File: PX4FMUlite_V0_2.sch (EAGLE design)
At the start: 150 parts, among them J2 DF13-4P-1.25V, J201 DF13C-6P-1.25V, J202 DF13C-6P-1.25V, J203 DF13C-6P-1.25V, J301 47346-0001, J302 DF13C-4P-1.25V, J401 DF13C-4P-1.25V, J403 DF13C-7P-1.25V, J404 DF13C-5P-1.25V, J405 DF13C-4P-1.25V, J801 JST-ZH-3, J802 DF13C-3P-1.25V, M3_MOUNT1101 MOUNT-HOLE3.1MM, M3_MOUNT1102 MOUNT-HOLE3.1MM, M3_MOUNT1103 MOUNT-HOLE3.1MM, M3_MOUNT1104 MOUNT-HOLE3.1MM, U1 MPU-6000QFN-24, U101 STM32F4X7VX, U401 MAX3051, U903 74LVC2G240, X101 3.2x2.5 mm / 24 MHz / 15 ppm

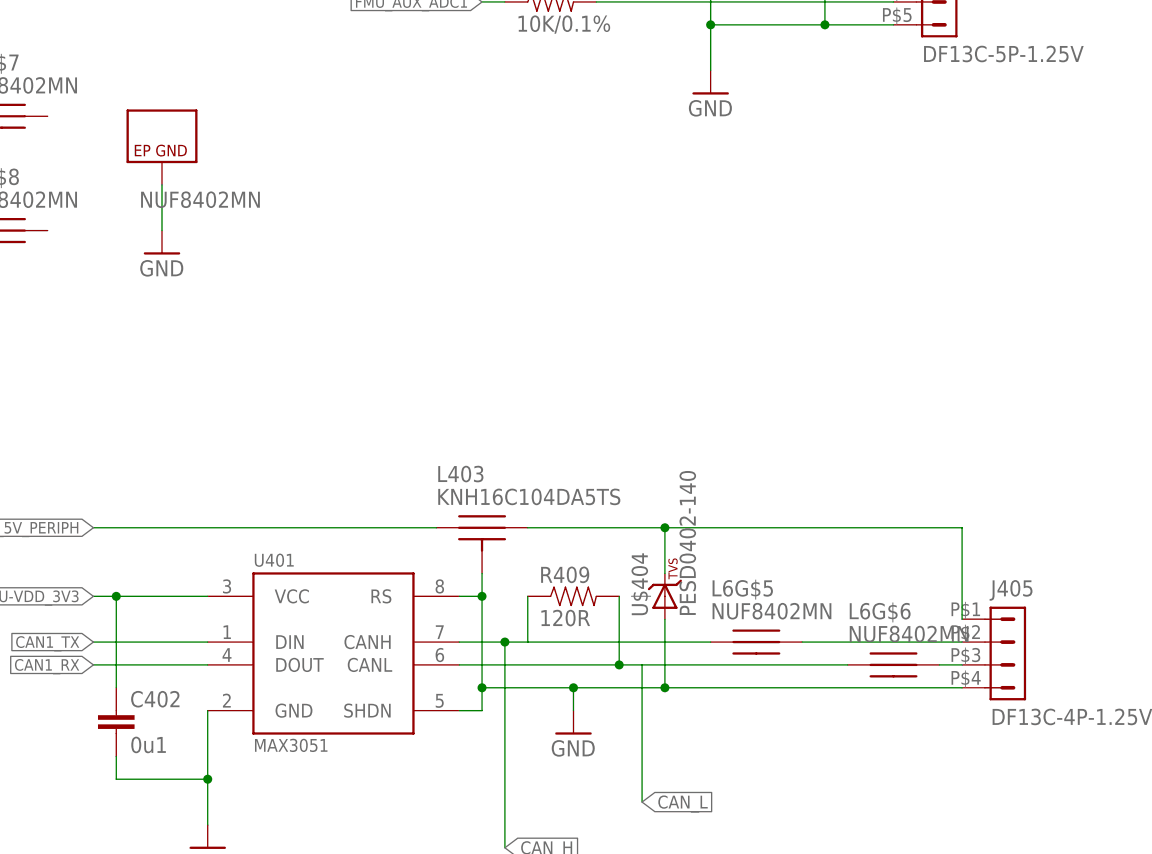
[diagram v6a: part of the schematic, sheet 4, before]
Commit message: USB connector move to side. UART conns together
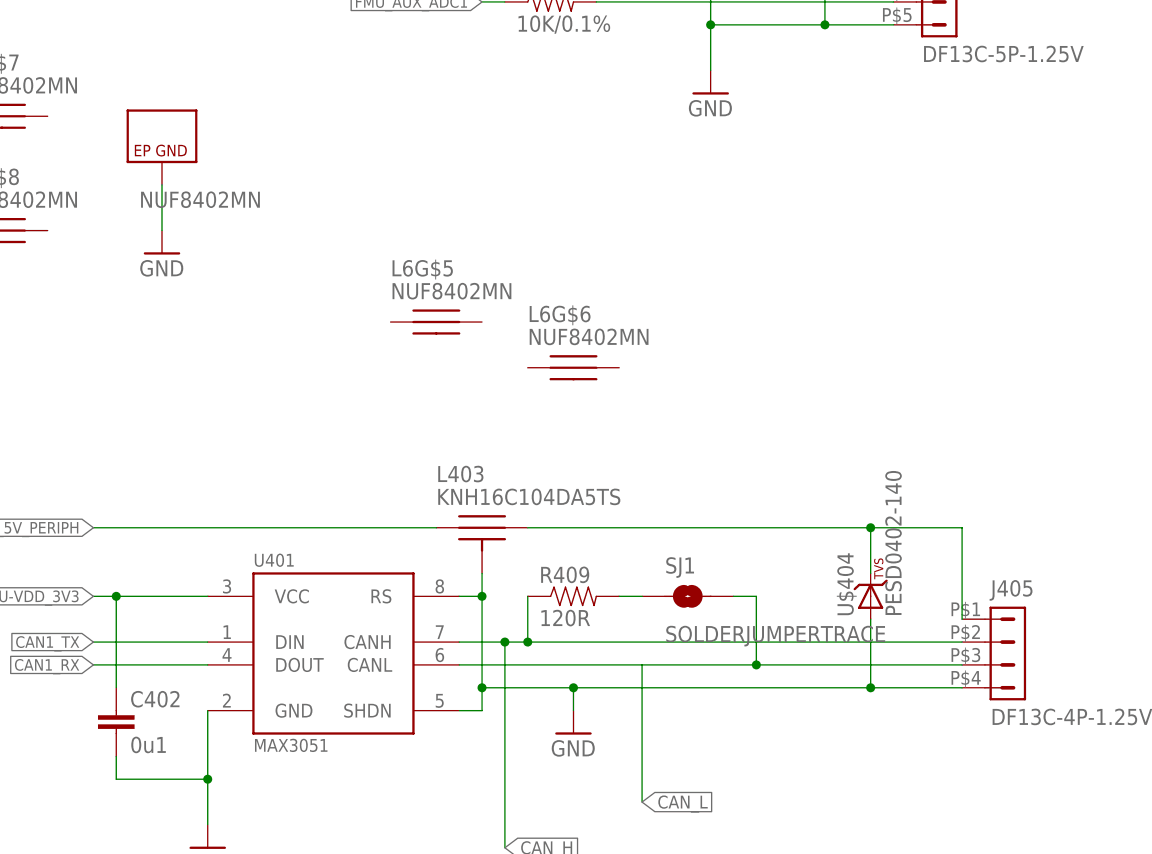
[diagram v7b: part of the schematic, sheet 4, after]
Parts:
- added SJ1: SOLDERJUMPERTRACE, SparkFun-Passives:SOLDERJUMPERTRACE
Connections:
- removed net N$24: J405.2, L6G$5.P$2
- net CAN_H: now also J405.2; no longer L6G$5.P$1
- net CAN_L: now also J405.3, SJ1.2; no longer L6G$6.P$1, R409.2
- net FMU-CH1: now also L1G$1.P$1
- net FMU-CH2: now also L1G$2.P$1
- net FMU-CH3: now also L1G$3.P$1
- net FMU-CH4: now also L1G$4.P$1
- net FMU-CH5: now also L1G$5.P$1
- net FMU-CH8: now also L1G$6.P$1
- net GND: now also L1G$9.GND, L2G$9.GND, L3G$9.GND
- net N$16: now also L1G$7.P$2
- net N$22: now also R409.2, SJ1.1; no longer J405.3, L6G$6.P$2
- net N$68: now also L1G$5.P$2
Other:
- moved on the sheet: L1G$5, L1G$7, L1G$8, L6G$5, L6G$6, U$404
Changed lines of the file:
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@@
 <part name="GND17" library="pixhawk2" deviceset="GND" device=""/>
 <part name="L6" library="PX4lite" deviceset="NUF8402MN" device=""/>
+<part name="SJ1" library="SparkFun-Passives" deviceset="SOLDERJUMPER" device="TRACE"/>
 </parts>
 <sheets>
@@
 <pinref part="GND8" gate="1" pin="GND"/>
 <wire x1="33.02" y1="111.76" x2="33.02" y2="116.84" width="0.1524" layer="91"/>
+<pinref part="L2" gate="G$9" pin="GND"/>
 </segment>
 <segment>
 <pinref part="GND9" gate="1" pin="GND"/>
 <wire x1="45.72" y1="22.86" x2="45.72" y2="27.94" width="0.1524" layer="91"/>
+<pinref part="L3" gate="G$9" pin="GND"/>
 </segment>
 </net>
@@
 <attribute name="PARTNO" x="220.98" y="152.4" size="1.778" layer="96" display="off"/>
 </instance>
-<instance part="U$404" gate="G$1" x="203.2" y="76.2" rot="R90">
-<attribute name="PARTNO" x="203.2" y="76.2" size="1.778" layer="96" display="off"/>
+<instance part="U$404" gate="G$1" x="226.06" y="76.2" rot="R90">
+<attribute name="PARTNO" x="226.06" y="76.2" size="1.778" layer="96" display="off"/>
 </instance>
 <instance part="U$401" gate="G$1" x="86.36" y="30.48" rot="R90">
@@
 <instance part="L6" gate="G$4" x="68.58" y="20.32"/>
 <instance part="L6" gate="G$9" x="147.32" y="121.92"/>
-<instance part="L6" gate="G$5" x="213.36" y="71.12"/>
-<instance part="L6" gate="G$6" x="228.6" y="68.58"/>
+<instance part="L6" gate="G$5" x="177.8" y="106.68"/>
+<instance part="L6" gate="G$6" x="193.04" y="101.6"/>
 <instance part="L6" gate="G$7" x="129.54" y="129.54"/>
 <instance part="L6" gate="G$8" x="129.54" y="116.84"/>
+<instance part="SJ1" gate="1" x="205.74" y="76.2"/>
 </instances>
 <busses>
@@
 </segment>
 <segment>
-<wire x1="236.22" y1="66.04" x2="203.2" y2="66.04" width="0.1524" layer="91"/>
-<wire x1="203.2" y1="66.04" x2="193.04" y2="66.04" width="0.1524" layer="91"/>
+<wire x1="236.22" y1="66.04" x2="226.06" y2="66.04" width="0.1524" layer="91"/>
+<wire x1="226.06" y1="66.04" x2="193.04" y2="66.04" width="0.1524" layer="91"/>
 <wire x1="193.04" y1="66.04" x2="193.04" y2="63.5" width="0.1524" layer="91"/>
 <wire x1="180.34" y1="76.2" x2="182.88" y2="76.2" width="0.1524" layer="91"/>
@@
 <junction x="182.88" y="76.2"/>
 <pinref part="U$404" gate="G$1" pin="A"/>
-<wire x1="203.2" y1="73.66" x2="203.2" y2="66.04" width="0.1524" layer="91"/>
-<junction x="203.2" y="66.04"/>
+<wire x1="226.06" y1="73.66" x2="226.06" y2="66.04" width="0.1524" layer="91"/>
+<junction x="226.06" y="66.04"/>
 </segment>
 <segment>
@@
 <junction x="185.42" y="71.12"/>
 <label x="185.42" y="48.26" size="1.4224" layer="95" xref="yes"/>
-<wire x1="208.28" y1="71.12" x2="187.96" y2="71.12" width="0.1524" layer="91"/>
-<pinref part="L6" gate="G$5" pin="P$1"/>
+<pinref part="J405" gate="G$1" pin="2"/>
+<wire x1="187.96" y1="71.12" x2="236.22" y2="71.12" width="0.1524" layer="91"/>
+<junction x="187.96" y="71.12"/>
 </segment>
 </net>
 <net name="CAN_L" class="0">
 <segment>
-<wire x1="198.12" y1="68.58" x2="180.34" y2="68.58" width="0.1524" layer="91"/>
-<wire x1="198.12" y1="76.2" x2="198.12" y2="68.58" width="0.1524" layer="91"/>
-<junction x="198.12" y="68.58"/>
-<pinref part="R409" gate="G$1" pin="2"/>
+<wire x1="200.66" y1="68.58" x2="180.34" y2="68.58" width="0.1524" layer="91"/>
 <pinref part="U401" gate="G$1" pin="CANL"/>
-<wire x1="200.66" y1="68.58" x2="198.12" y2="68.58" width="0.1524" layer="91"/>
 <wire x1="200.66" y1="68.58" x2="200.66" y2="53.34" width="0.1524" layer="91"/>
 <label x="200.66" y="53.34" size="1.4224" layer="95" xref="yes"/>
-<wire x1="200.66" y1="68.58" x2="223.52" y2="68.58" width="0.1524" layer="91"/>
-<pinref part="L6" gate="G$6" pin="P$1"/>
+<pinref part="J405" gate="G$1" pin="3"/>
+<wire x1="200.66" y1="68.58" x2="213.36" y2="68.58" width="0.1524" layer="91"/>
+<pinref part="SJ1" gate="1" pin="2"/>
+<wire x1="213.36" y1="68.58" x2="236.22" y2="68.58" width="0.1524" layer="91"/>
+<wire x1="210.82" y1="76.2" x2="213.36" y2="76.2" width="0.1524" layer="91"/>
+<wire x1="213.36" y1="76.2" x2="213.36" y2="68.58" width="0.1524" layer="91"/>
+<junction x="213.36" y="68.58"/>
 </segment>
 </net>
@@
 <wire x1="236.22" y1="73.66" x2="236.22" y2="83.82" width="0.1524" layer="91"/>
 <pinref part="L403" gate="G$1" pin="P$2"/>
-<wire x1="236.22" y1="83.82" x2="203.2" y2="83.82" width="0.1524" layer="91"/>
+<wire x1="236.22" y1="83.82" x2="226.06" y2="83.82" width="0.1524" layer="91"/>
 <pinref part="U$404" gate="G$1" pin="C"/>
-<wire x1="203.2" y1="83.82" x2="187.96" y2="83.82" width="0.1524" layer="91"/>
-<wire x1="203.2" y1="78.74" x2="203.2" y2="83.82" width="0.1524" layer="91"/>
-<junction x="203.2" y="83.82"/>
+<wire x1="226.06" y1="83.82" x2="187.96" y2="83.82" width="0.1524" layer="91"/>
+<wire x1="226.06" y1="78.74" x2="226.06" y2="83.82" width="0.1524" layer="91"/>
+<junction x="226.06" y="83.82"/>
 </segment>
 </net>
@@
 <net name="N$22" class="0">
 <segment>
-<pinref part="J405" gate="G$1" pin="3"/>
-<wire x1="233.68" y1="68.58" x2="236.22" y2="68.58" width="0.1524" layer="91"/>
-<pinref part="L6" gate="G$6" pin="P$2"/>
-</segment>
-</net>
-<net name="N$24" class="0">
-<segment>
-<pinref part="J405" gate="G$1" pin="2"/>
-<wire x1="236.22" y1="71.12" x2="218.44" y2="71.12" width="0.1524" layer="91"/>
-<pinref part="L6" gate="G$5" pin="P$2"/>
+<pinref part="R409" gate="G$1" pin="2"/>
+<pinref part="SJ1" gate="1" pin="1"/>
+<wire x1="198.12" y1="76.2" x2="200.66" y2="76.2" width="0.1524" layer="91"/>
 </segment>
 </net>
@@
 <instance part="L1" gate="G$3" x="53.34" y="109.22"/>
 <instance part="L1" gate="G$4" x="81.28" y="114.3"/>
-<instance part="L1" gate="G$5" x="68.58" y="119.38"/>
+<instance part="L1" gate="G$5" x="66.04" y="119.38"/>
 <instance part="L1" gate="G$6" x="53.34" y="124.46"/>
-<instance part="L1" gate="G$7" x="81.28" y="129.54"/>
-<instance part="L1" gate="G$8" x="68.58" y="134.62"/>
-<instance part="L1" gate="G$9" x="53.34" y="88.9"/>
+<instance part="L1" gate="G$7" x="78.74" y="129.54"/>
+<instance part="L1" gate="G$8" x="66.04" y="134.62"/>
 <instance part="GND5" gate="1" x="53.34" y="81.28"/>
 <instance part="J1" gate="-CH10" x="101.6" y="144.78"/>
+<instance part="L1" gate="G$9" x="53.34" y="88.9"/>
 </instances>
 <busses>
@@
 <wire x1="40.64" y1="99.06" x2="76.2" y2="99.06" width="0.1524" layer="91"/>
 <label x="40.64" y="99.06" size="1.27" layer="95" rot="R180" xref="yes"/>
+<pinref part="L1" gate="G$1" pin="P$1"/>
 </segment>
 </net>
@@
 <wire x1="40.64" y1="104.14" x2="63.5" y2="104.14" width="0.1524" layer="91"/>
 <label x="40.64" y="104.14" size="1.27" layer="95" rot="R180" xref="yes"/>
+<pinref part="L1" gate="G$2" pin="P$1"/>
 </segment>
 </net>
@@
 <wire x1="40.64" y1="109.22" x2="48.26" y2="109.22" width="0.1524" layer="91"/>
 <label x="40.64" y="109.22" size="1.27" layer="95" rot="R180" xref="yes"/>
+<pinref part="L1" gate="G$3" pin="P$1"/>
 </segment>
 </net>
@@
 <pinref part="J1" gate="-CH5" pin="S"/>
 <wire x1="71.12" y1="119.38" x2="99.06" y2="119.38" width="0.1524" layer="91"/>
+<pinref part="L1" gate="G$5" pin="P$2"/>
 </segment>
 </net>
@@
 <wire x1="40.64" y1="114.3" x2="76.2" y2="114.3" width="0.1524" layer="91"/>
 <label x="40.64" y="114.3" size="1.27" layer="95" rot="R180" xref="yes"/>
+<pinref part="L1" gate="G$4" pin="P$1"/>
 </segment>
 </net>
 <net name="FMU-CH5" class="0">
 <segment>
-<wire x1="40.64" y1="119.38" x2="63.5" y2="119.38" width="0.1524" layer="91"/>
+<wire x1="40.64" y1="119.38" x2="60.96" y2="119.38" width="0.1524" layer="91"/>
 <label x="40.64" y="119.38" size="1.27" layer="95" rot="R180" xref="yes"/>
+<pinref part="L1" gate="G$5" pin="P$1"/>
 </segment>
 </net>
@@
 <label x="40.64" y="129.54" size="1.27" layer="95" rot="R180" xref="yes"/>
 <label x="40.64" y="134.62" size="1.27" layer="95" rot="R180" xref="yes"/>
+<pinref part="L1" gate="G$6" pin="P$1"/>
 </segment>
 </net>
@@
 <pinref part="J1" gate="-CH8" pin="S"/>
 <pinref part="L1" gate="G$8" pin="P$2"/>
-<wire x1="73.66" y1="134.62" x2="99.06" y2="134.62" width="0.1524" layer="91"/>
+<wire x1="71.12" y1="134.62" x2="99.06" y2="134.62" width="0.1524" layer="91"/>
 </segment>
 </net>
@@
 <pinref part="J1" gate="-CH7" pin="S"/>
 <wire x1="83.82" y1="129.54" x2="99.06" y2="129.54" width="0.1524" layer="91"/>
+<pinref part="L1" gate="G$7" pin="P$2"/>
 </segment>
 </net>
@@
 <segment>
 <pinref part="L1" gate="G$7" pin="P$1"/>
-<wire x1="76.2" y1="129.54" x2="40.64" y2="129.54" width="0.1524" layer="91"/>
+<wire x1="73.66" y1="129.54" x2="40.64" y2="129.54" width="0.1524" layer="91"/>
 </segment>
 </net>
@@
 </segment>
 </net>
-<net name="GND" class="0">
+<net name="N$18" class="0">
 <segment>
-<pinref part="GND5" gate="1" pin="GND"/>
-<wire x1="53.34" y1="83.82" x2="53.34" y2="88.9" width="0.1524" layer="91"/>
+<pinref part="L1" gate="G$8" pin="P$1"/>
+<wire x1="60.96" y1="134.62" x2="40.64" y2="134.62" width="0.1524" layer="91"/>
 </segment>
 </net>
-<net name="N$18" class="0">
+<net name="GND" class="0">
 <segment>
-<pinref part="L1" gate="G$8" pin="P$1"/>
-<wire x1="63.5" y1="134.62" x2="40.64" y2="134.62" width="0.1524" layer="91"/>
+<pinref part="GND5" gate="1" pin="GND"/>
+<wire x1="53.34" y1="83.82" x2="53.34" y2="88.9" width="0.1524" layer="91"/>
+<pinref part="L1" gate="G$9" pin="GND"/>
 </segment>
 </net>

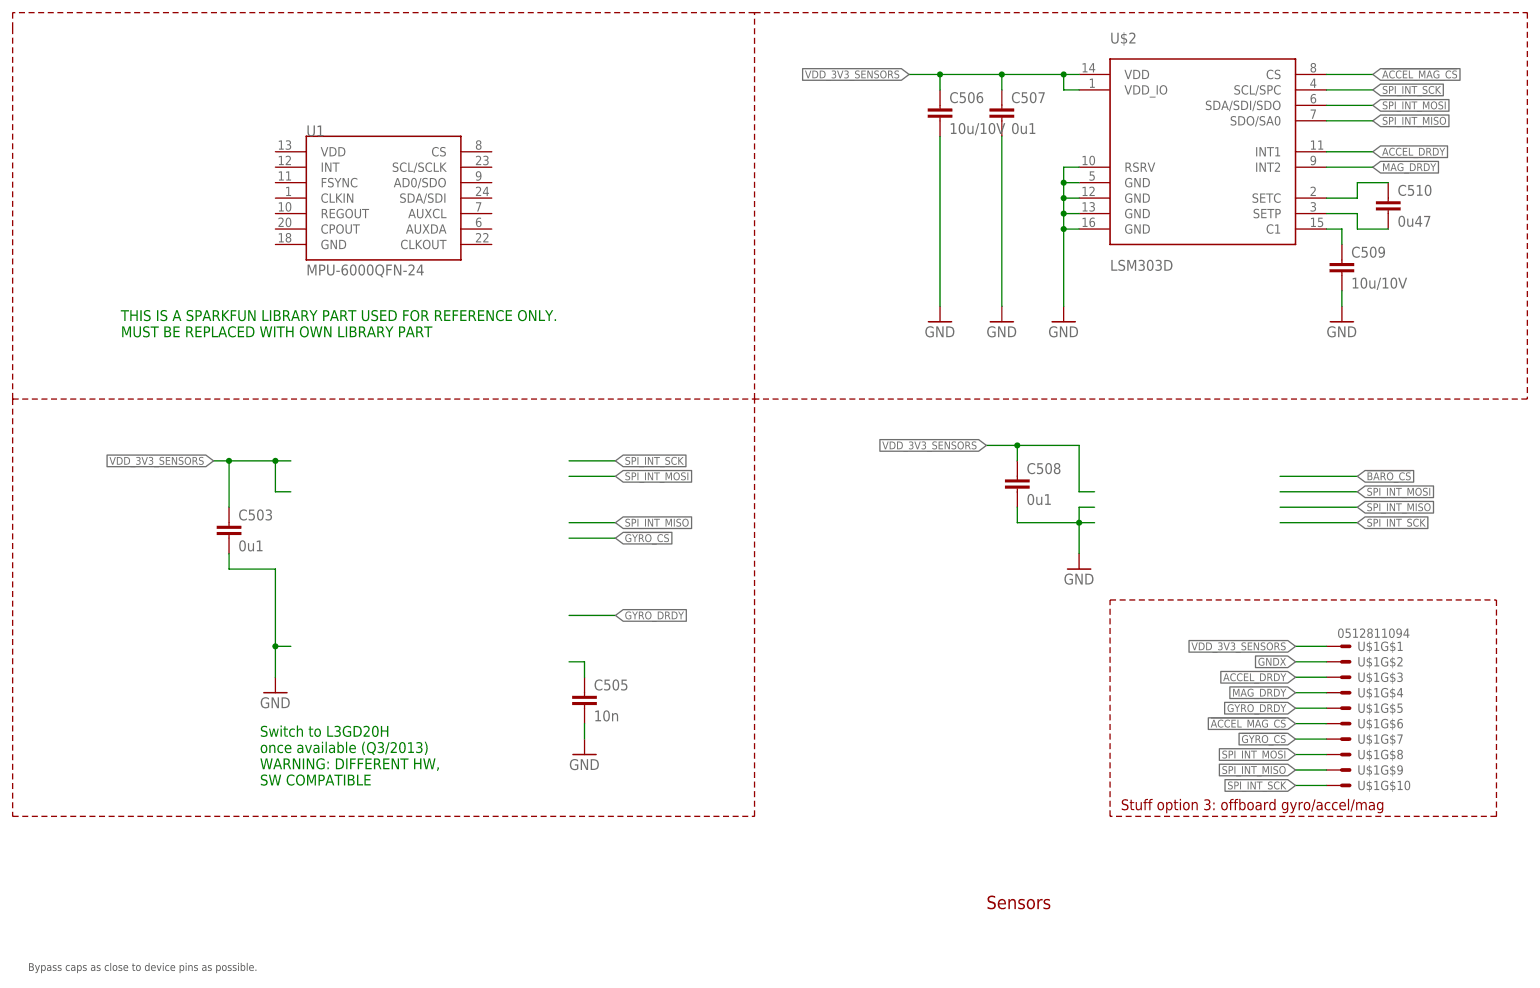
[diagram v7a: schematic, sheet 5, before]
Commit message: Tweaks on MPU6000
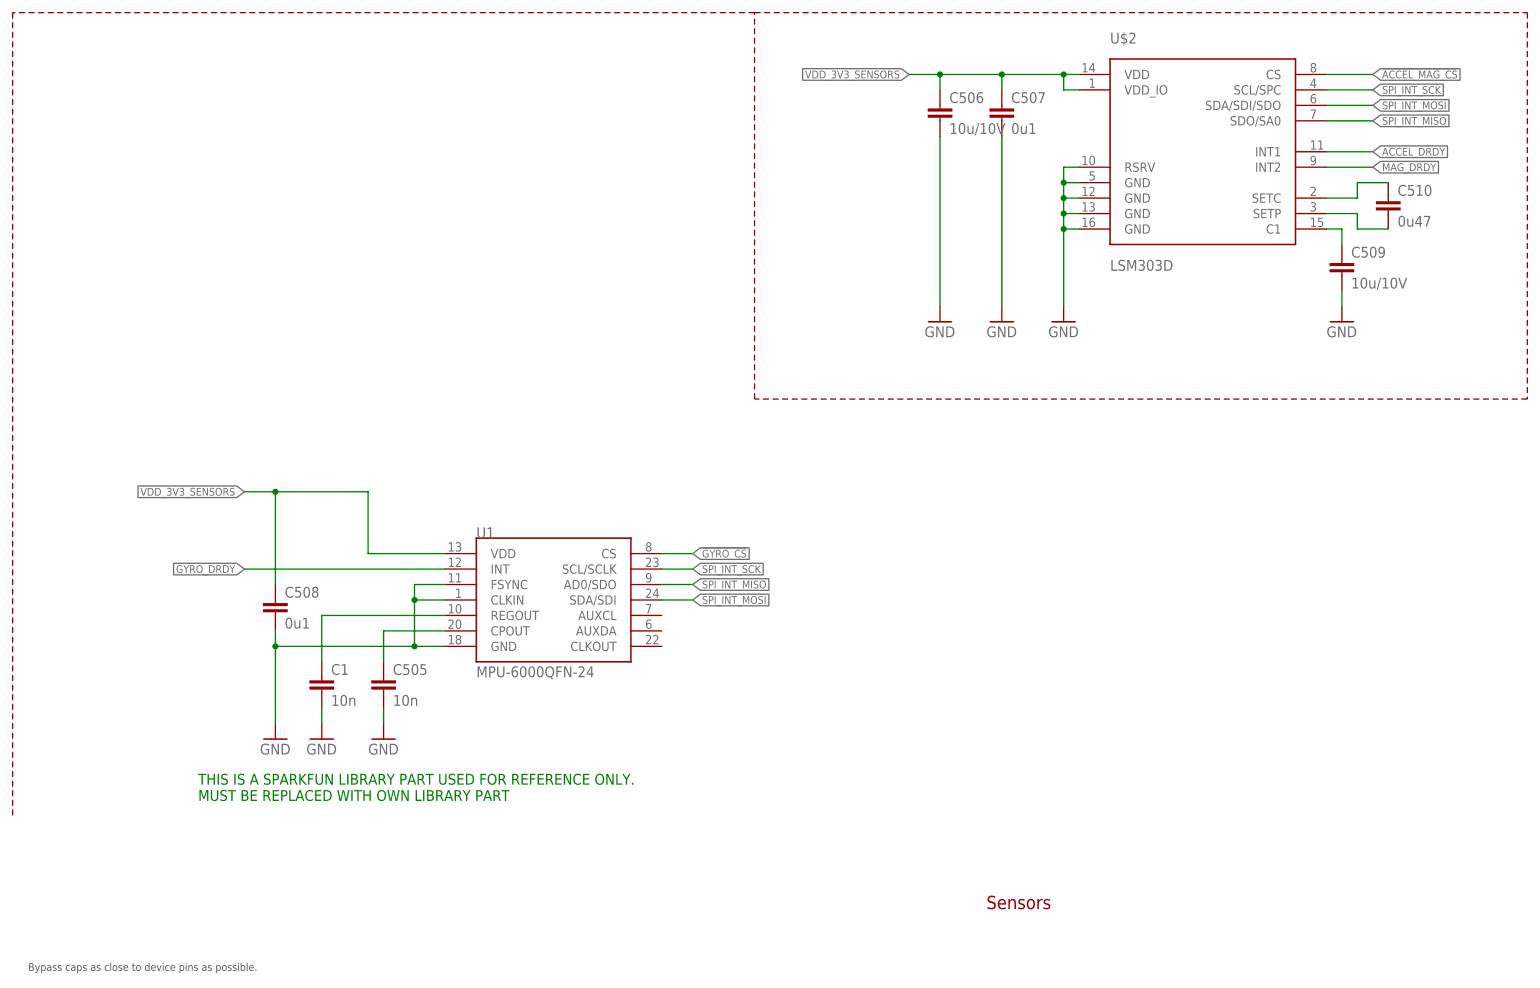
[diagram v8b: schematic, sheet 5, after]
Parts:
- removed C503: 0u1, pixhawk2:CAP0402
- removed LED702: GREEN, pixhawk2:LED0603
- removed LED703: AMBER, pixhawk2:LED0603
- removed R4, R708, R709: 220R, pixhawk2:RESISTOR0402-RES
- removed U$1: 0512811094, pixhawk2:CONN_FPC_10RA
- added C1: 10n, pixhawk2:CAP0402
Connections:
- net !IO-LED_BLUE renamed FMU-LED_BLUE
- net !IO-LED_SAFETY renamed FMU-LED_SAFETY
- removed net !IO-LED_AMBER: R709.1
- removed net N$29: LED702.C, R708.2
- removed net N$30: C505.1
- removed net N$39: R4.1, R709.2
- removed net N$40: LED703.C, R4.2
- new net N$24: LED705.A
- new net N$25: C505.1, U1.CPOUT
- new net N$27: C1.1, U1.REGOUT
- net !ACCEL_MAG_CS: no longer U$1G$6.S
- net !GYRO_CS: now also U1.CS; no longer U$1G$7.S
- net ACCEL_DRDY: no longer U$1G$3.S
- net FMU-VDD_3V3: now also J802.1, U$701.C
- net FMU-VDD_5V: no longer LED702.A, LED703.A, LED705.A
- net GND: now also C1.2
- net GNDX: now also U1.CLKIN, U1.FSYNC, U1.GND; no longer C503.2, R708.1, U$1G$2.S
- net GYRO_DRDY: now also U1.INT; no longer U$1G$5.S
- net IO-VDD_3V3: no longer J802.1, U$701.C
- net MAG_DRDY: no longer U$1G$4.S
- net SPI_INT_MISO: now also U1.AD0/SDO; no longer U$1G$9.S
- net SPI_INT_MOSI: now also U1.SDA/SDI; no longer U$1G$8.S
- net SPI_INT_SCK: now also U1.SCL/SCLK; no longer U$1G$10.S
- net VDD_3V3_SENSORS: now also U1.VDD; no longer C503.1, U$1G$1.S
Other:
- note added: "PROTECT THIS VDD OUT"
- note removed: "Stuff option 3: offboard gyro/accel/mag"
- note removed: "Switch to L3GD20H once available (Q3/2013) WARNING: DIFFERENT HW, SW COMPATIBLE"
- moved on the sheet: C505, C508, U1
